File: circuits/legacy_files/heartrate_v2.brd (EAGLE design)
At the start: 21.3 x 10.5 mm, 21 parts

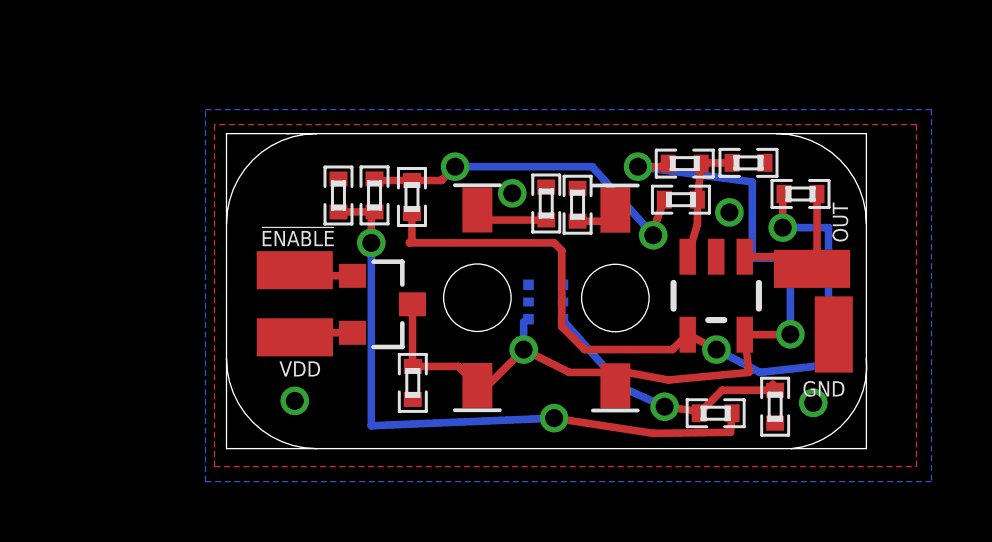
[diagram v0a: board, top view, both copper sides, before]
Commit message: remade heart rate sensor
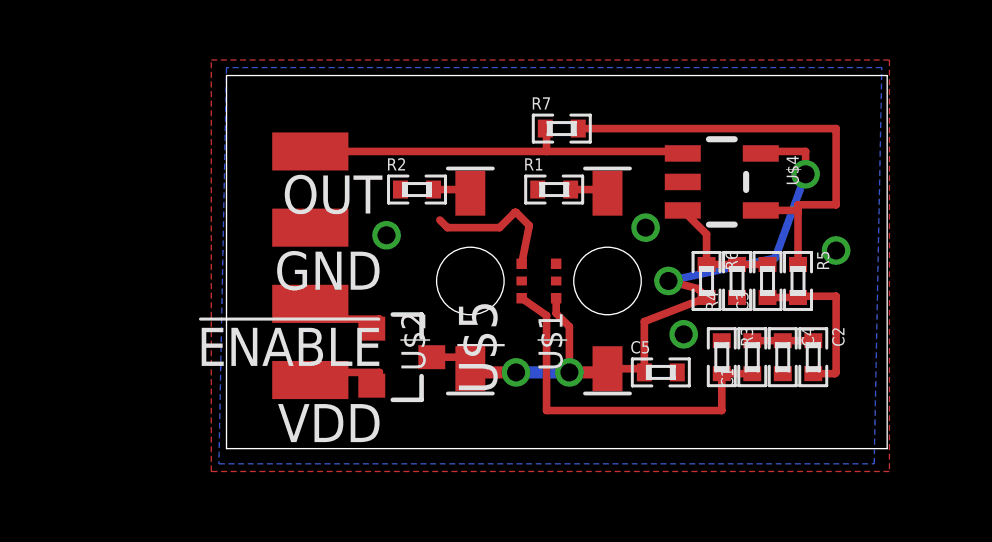
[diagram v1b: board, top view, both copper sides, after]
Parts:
- moved GND 17.8 mm to (2.79, 7.37), turned to 90 degrees
- moved OUT 17.2 mm to (2.79, 9.91)
- moved C4 15.8 mm to (18.5, 3.05), turned to 270 degrees
- moved C2 15.6 mm to (19.6, 3.05), turned to 270 degrees
- moved R5 13.2 mm to (19.1, 5.59), turned to 270 degrees
- moved C5 8.28 mm to (14.5, 2.54), turned to 0 degrees
- moved R7 8.25 mm to (11.2, 10.7), turned to 0 degrees
- moved R2 4.33 mm to (6.35, 8.64), turned to 0 degrees
- moved R6 3.98 mm to (16.0, 5.59), turned to 270 degrees
- moved C3 3.96 mm to (18.0, 5.59), turned to 90 degrees
- moved R4 3.96 mm to (17.0, 5.59), turned to 90 degrees
- moved U$4 3.80 mm to (16.5, 8.89), turned to 270 degrees
- moved R3 2.43 mm to (16.5, 3.05), turned to 270 degrees
- moved C1 2.23 mm to (17.5, 3.05), turned to 90 degrees
- moved U$5 1.88 mm to (5.84, 3.05)
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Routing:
- net N$6: track 21.0 -> 2.03 mm, vias 2 -> 0
- net VDD: track 30.1 -> 17.8 mm, vias 3 -> 2
- net N$12: track 25.7 -> 15.6 mm, vias 2 -> 0
- net OUT: track 4.89 -> 13.2 mm
- net N$17: track 0.00 -> 6.61 mm, vias 0 -> 2
- net N$7: track 11.8 -> 5.62 mm, vias 2 -> 0
- net GND: track 0.00 -> 5.54 mm
- net N$5: track 8.82 -> 12.3 mm, vias 1 -> 0
- net N$2: track 2.07 -> 3.57 mm
- net N$4: track 2.63 -> 1.35 mm
- net N$3: track 2.11 -> 3.22 mm
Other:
- board size 21.3 x 10.5 mm -> 22 x 12.4 mm
